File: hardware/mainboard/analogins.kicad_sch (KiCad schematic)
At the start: 23 parts, among them J102 CV A, J103 DUTY A, J111 CV B, J112 DUTY B, U13 MCP6004

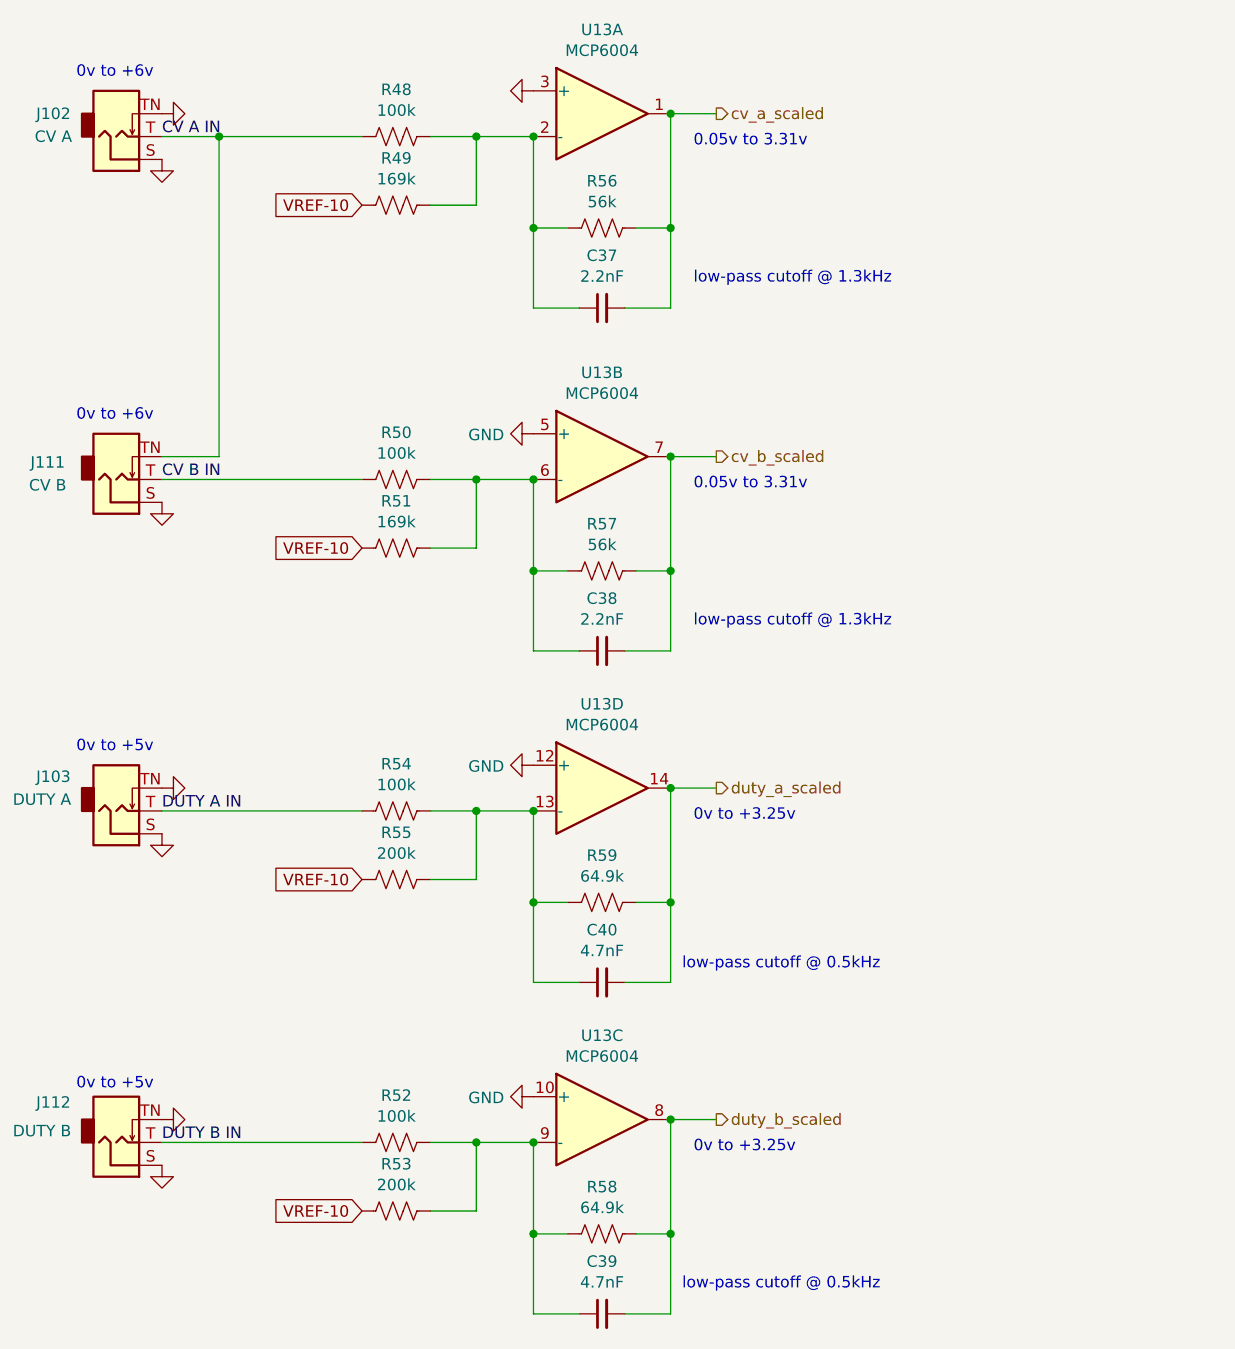
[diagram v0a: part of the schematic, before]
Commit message: Add ESD protection for inputs
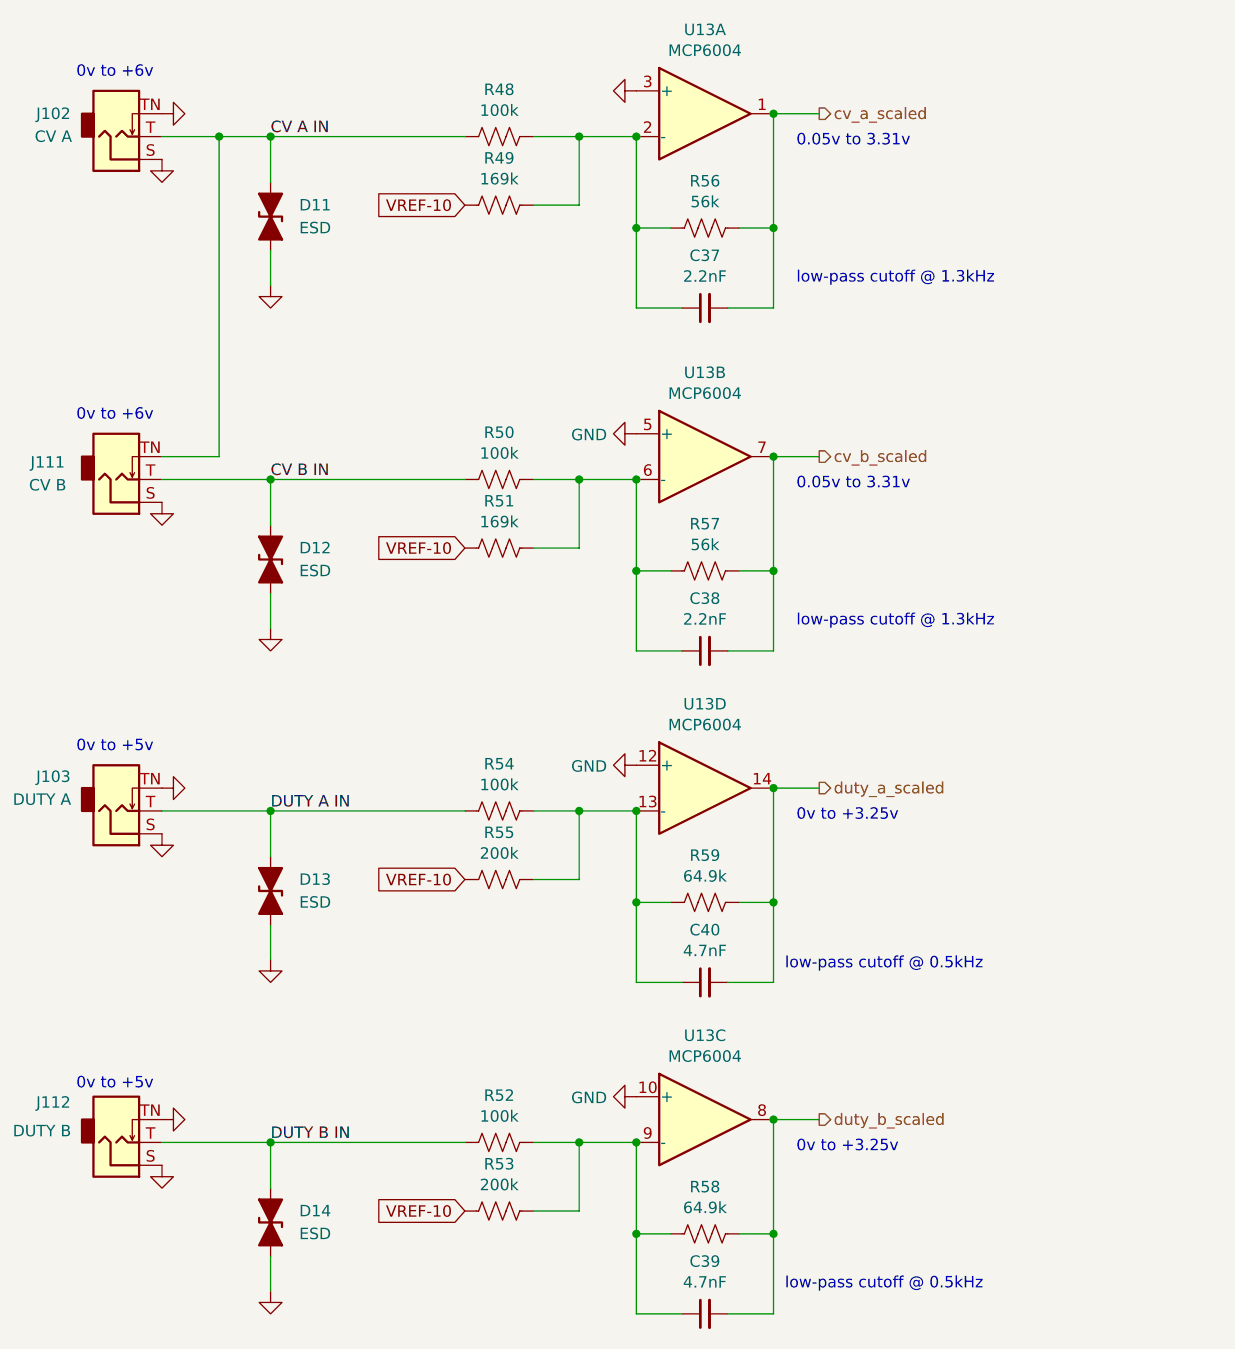
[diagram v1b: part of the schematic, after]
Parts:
- added D11, D12, D13, D14: ESD, Capacitor_SMD:C_0603_1608Metric_Pad1.08x0.95mm_HandSolder, symbol Device:D_TVS_Filled
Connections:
- net CV A IN: now also D11.2 (A2)
- net CV B IN: now also D12.2 (A2)
- net DUTY A IN: now also D13.2 (A2)
- net DUTY B IN: now also D14.2 (A2)
- net GND: now also D11.1 (A1), D12.1 (A1), D13.1 (A1), D14.1 (A1)
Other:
- moved on the sheet: C37, C38, C39, C40, R48, R49, R50, R51, R52, R53, R54, R55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

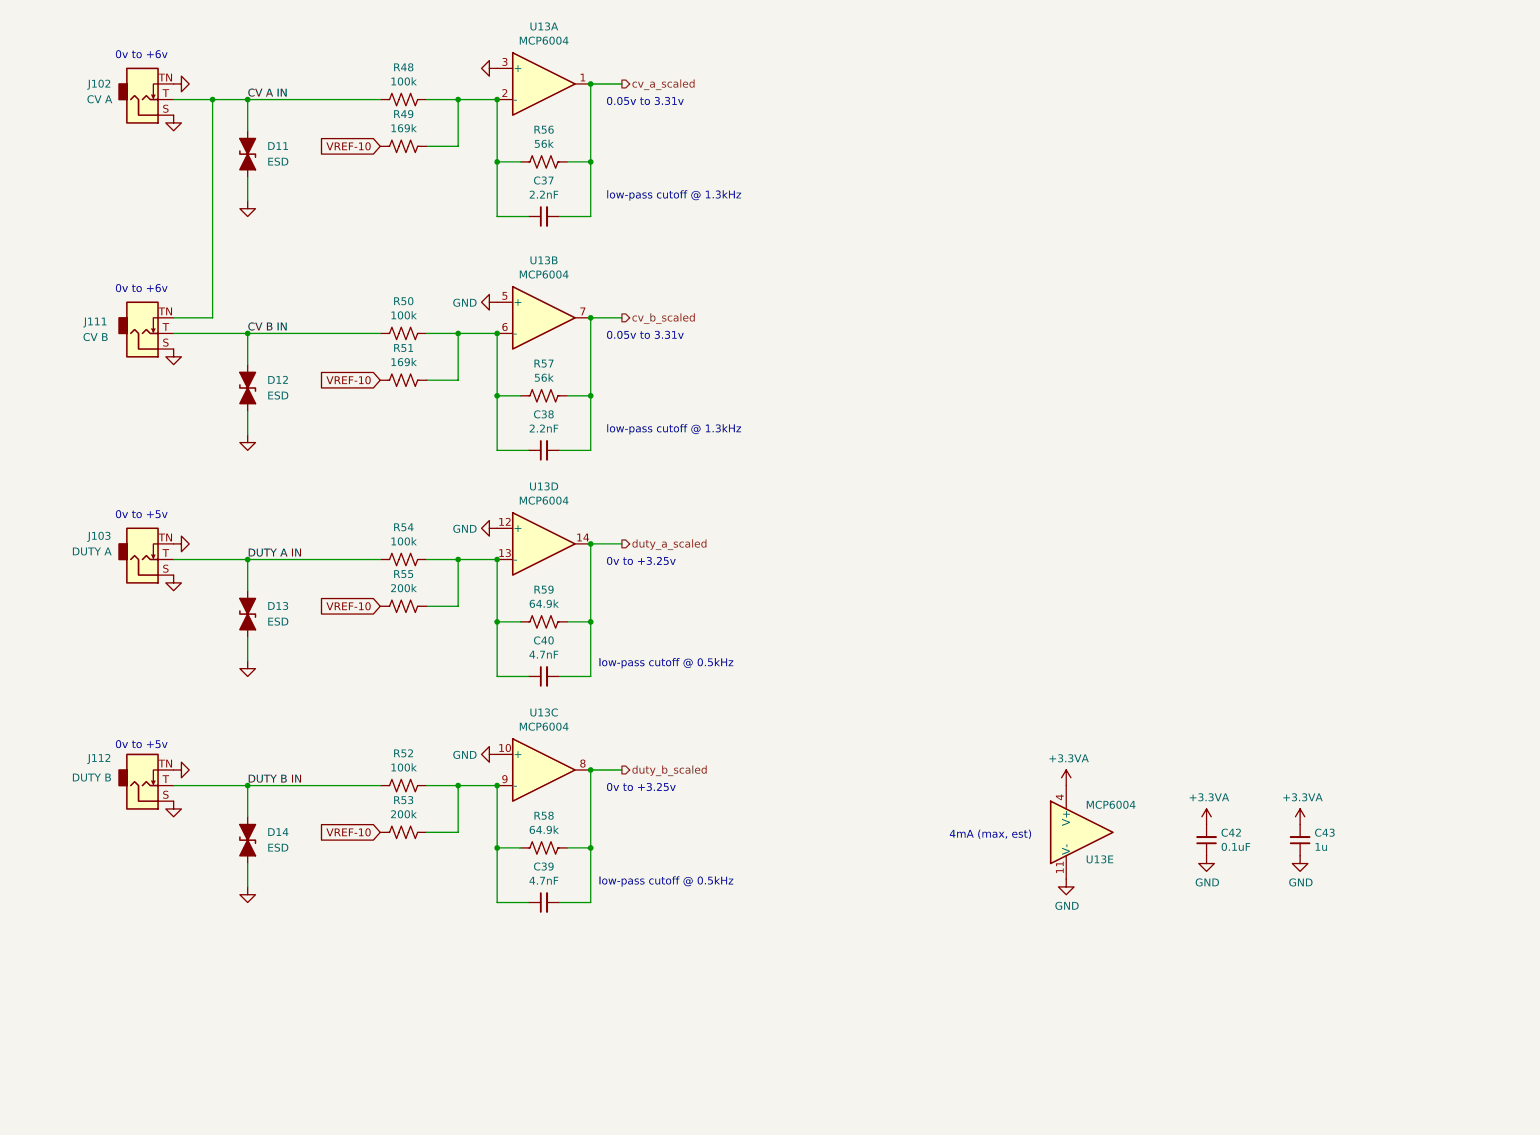
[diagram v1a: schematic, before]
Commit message: Progress on cleaning up the schematics
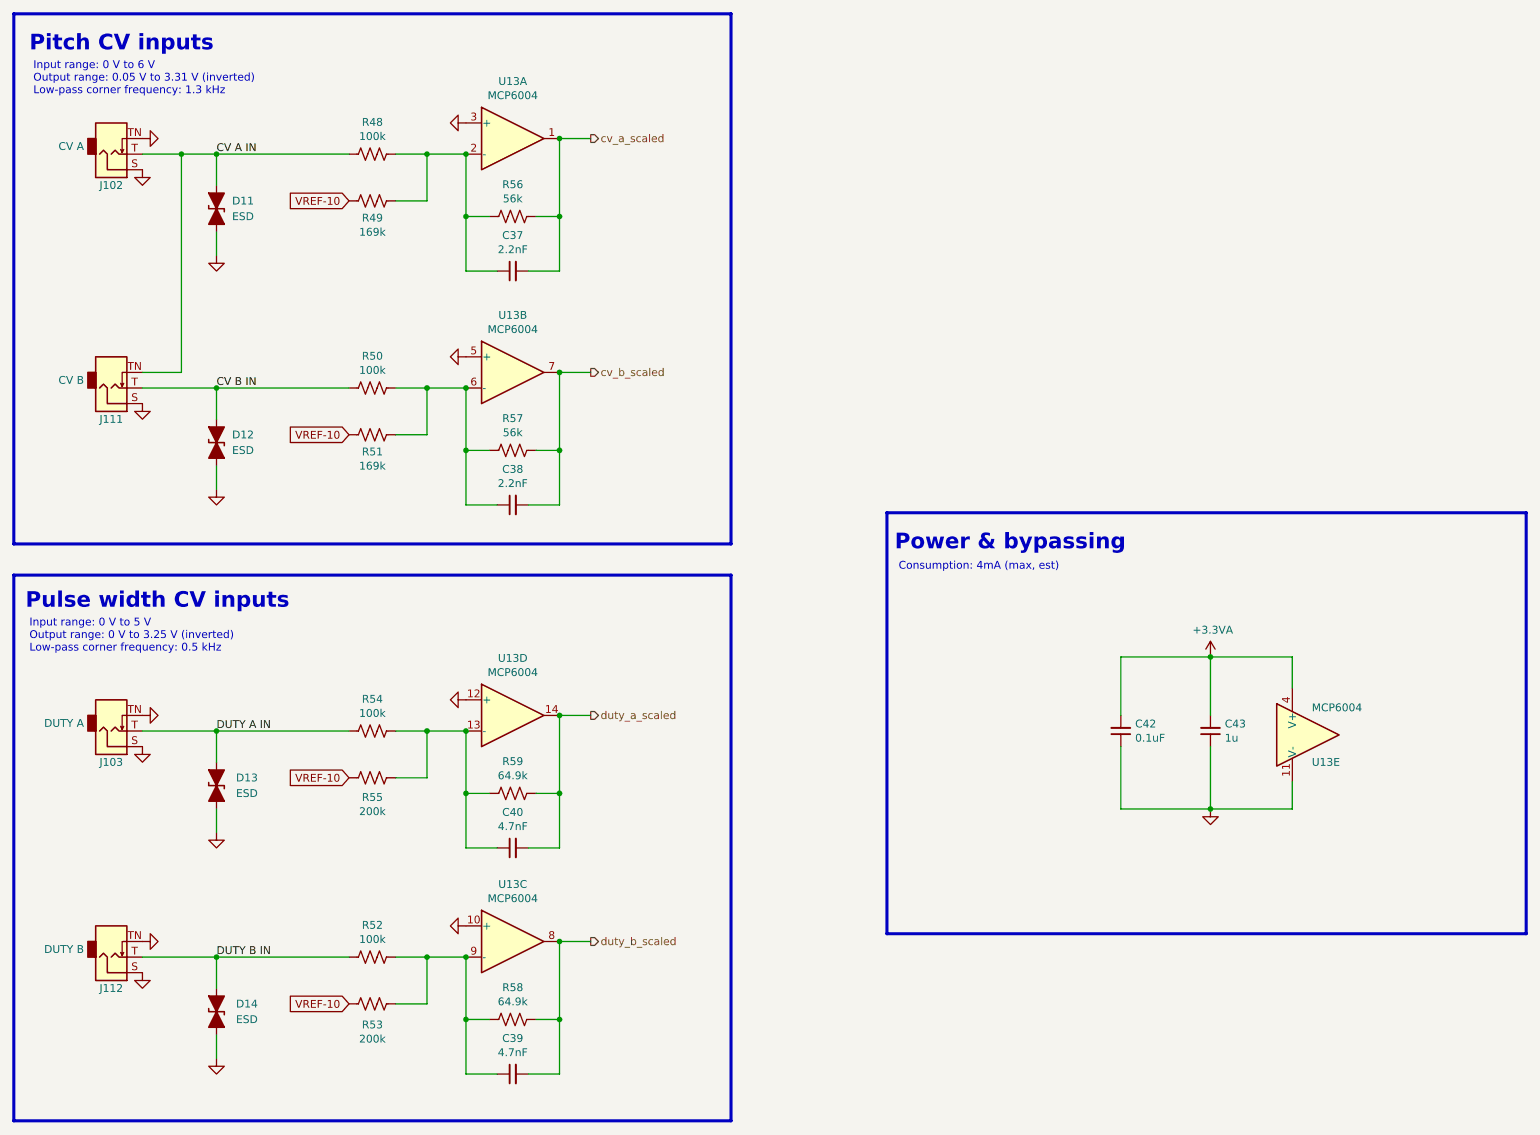
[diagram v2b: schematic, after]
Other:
- note added: "Consumption: 4mA (max, est)"
- note added: "Input range: 0 V to 5 V Output range: 0 V to 3.25 V (inverted) Low-pass corner frequency: 0.5 kHz"
- note added: "Input range: 0 V to 6 V Output range: 0.05 V to 3.31 V (inverted) Low-pass corner frequency: 1.3 kHz"
- note added: "Pitch CV inputs"
- note added: "Power & bypassing"
- note added: "Pulse width CV inputs"
- note removed: "0.05v to 3.31v"
- note removed: "0v to +3.25v"
- note removed: "0v to +5v"
- note removed: "0v to +6v"
- note removed: "4mA (max, est)"
- note removed: "low-pass cutoff @ 0.5kHz"
- note removed: "low-pass cutoff @ 1.3kHz"
- moved on the sheet: C37, C38, C39, C40, C42, C43, D11, D12, D13, D14, J102, J103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

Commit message: More schematic cleanup - nearly done!
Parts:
- J102: value CV A -> CASTOR PITCH
- J103: value DUTY A -> CASTOR DUTY
- J111: value CV B -> POLLUX PITCH
- J112: value DUTY B -> POLLUX DUTY
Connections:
- net cv_a_scaled renamed CASTOR_PITCH_CV
- net cv_b_scaled renamed POLLUX_PITCH_CV
- net duty_a_scaled renamed CASTOR_DUTY_CV
- net duty_b_scaled renamed POLLUX_DUTY_CV
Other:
- moved on the sheet: C37, C38, C39, C40, D11, D12, D13, D14, J102, J103, J111, J112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
